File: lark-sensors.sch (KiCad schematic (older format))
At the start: 17 parts, among them IC1 MS5611-01BA03, IC2 MS5611-01BA03, U5 PCA9544AD, U9 MS5525DSO

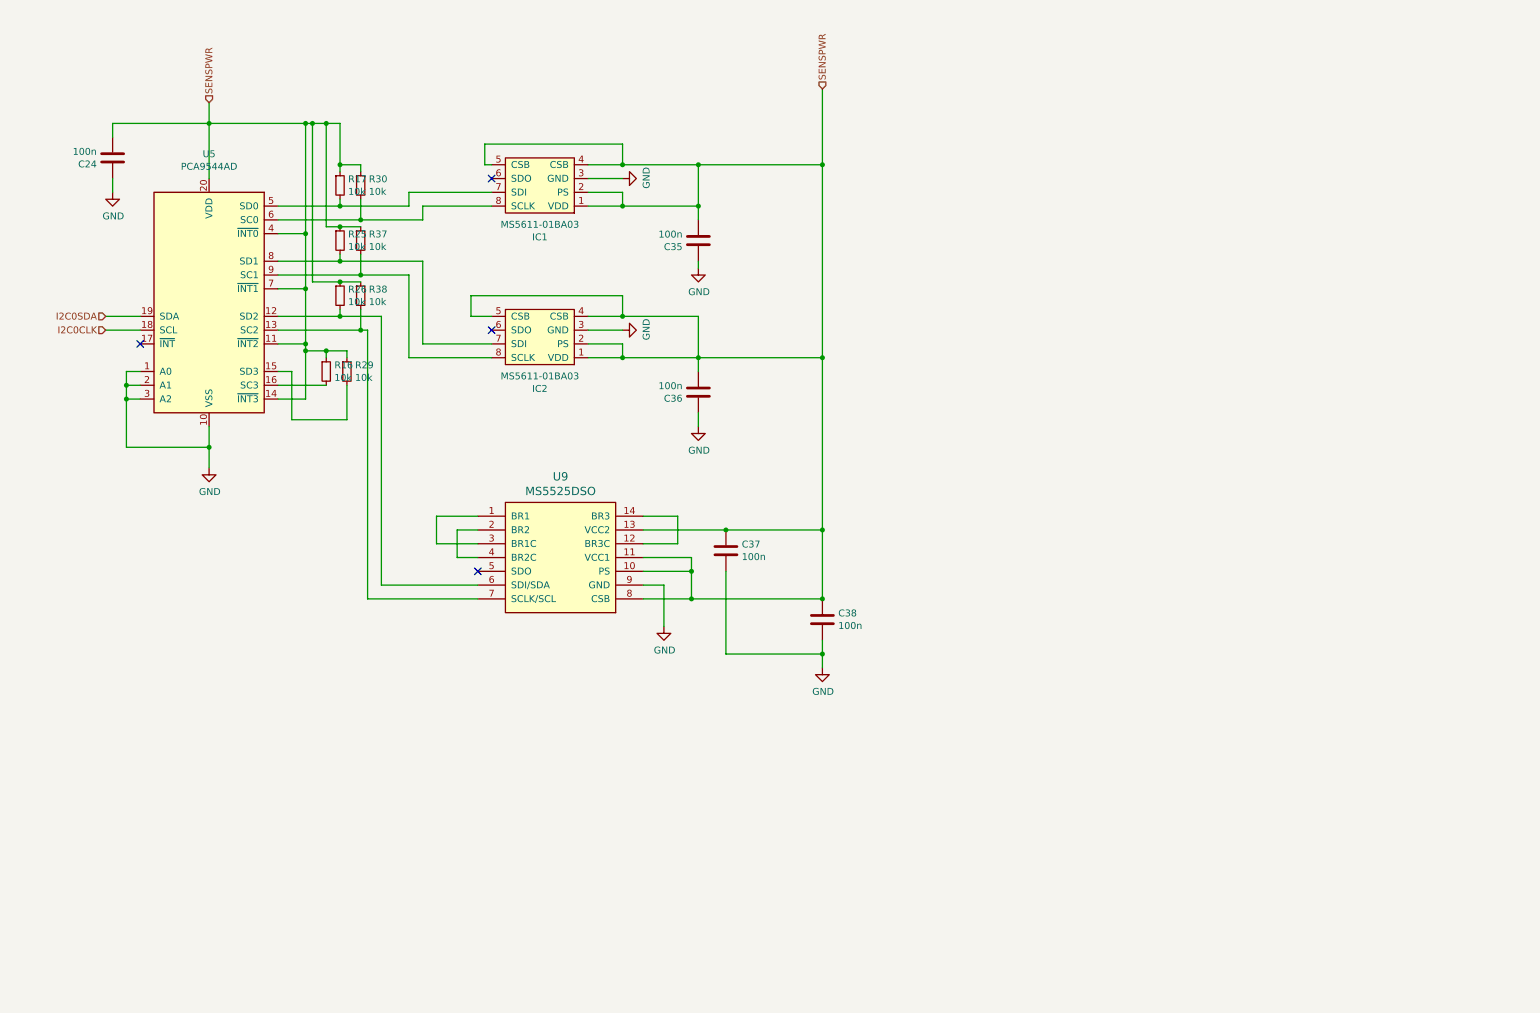
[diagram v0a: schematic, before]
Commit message: Fitting layout into 57 mm instrument.
* board width is 51 mm at the moment
* split into two boards (sensor and main) which can be stacked with
  2.54 mm pinheaders.
* ESP32 was put to bottom with optional pcb antenna facing to front.
* added footprint for optional HCLAxxE on sensorboard
* added footprint for BMI088

* Is multiple GND pins for sensor board really a good idea (ground loops)?
* Does the +12V topology make sense (especially regarding the external
  IGC ports)?
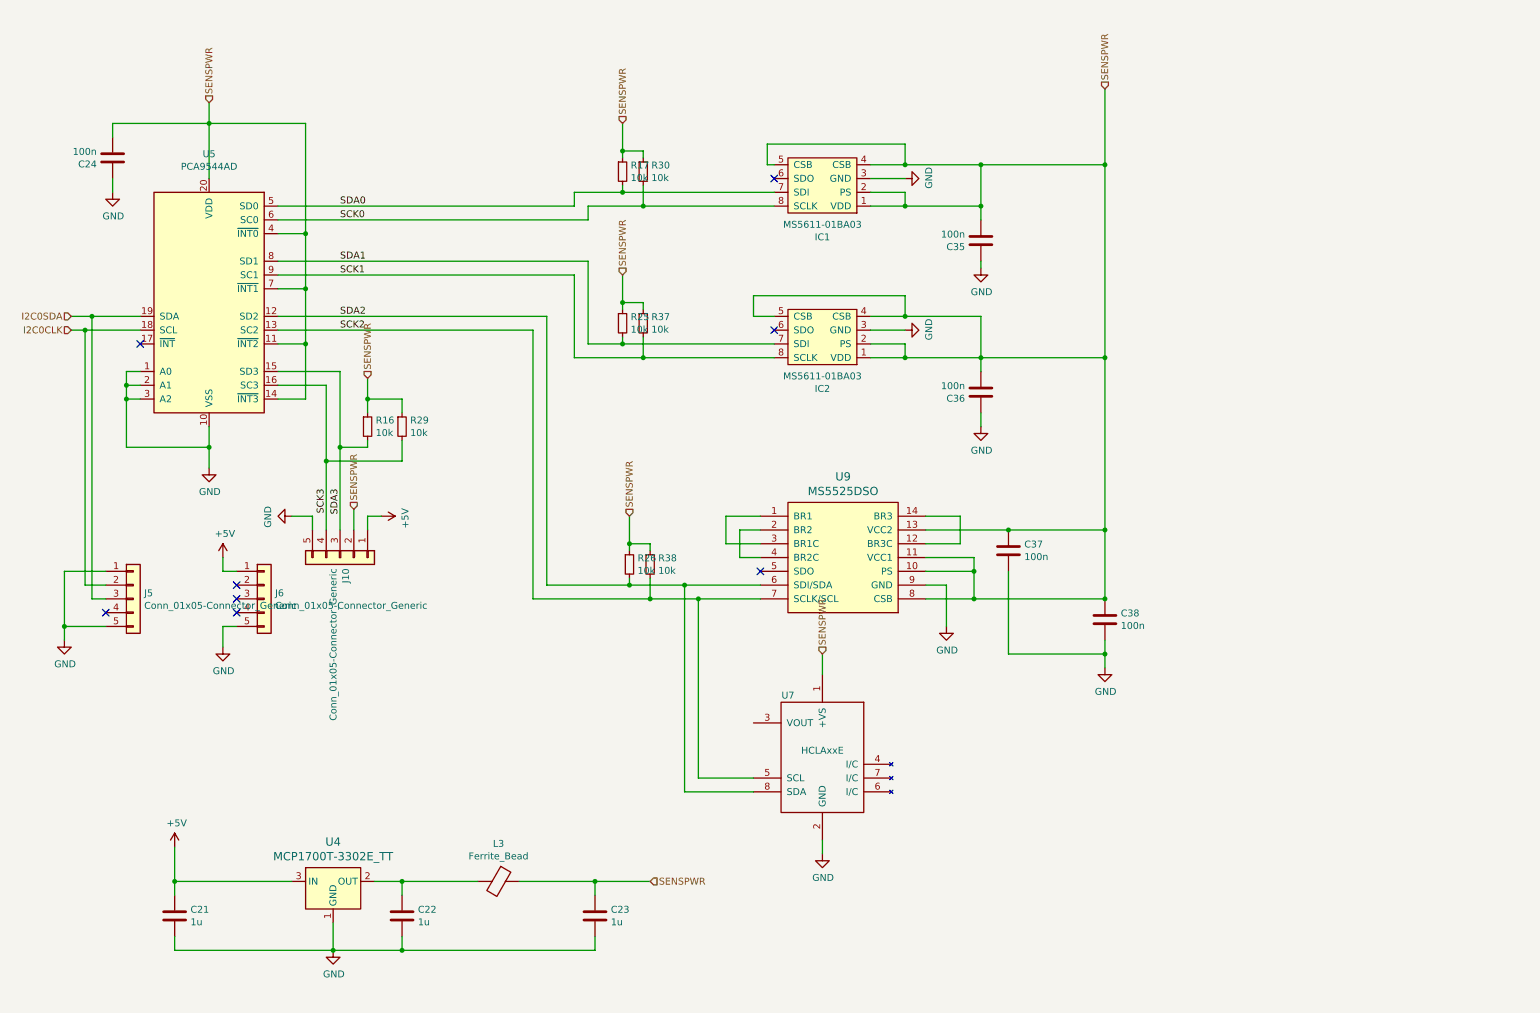
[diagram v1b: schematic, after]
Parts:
- added C21, C22, C23: 1u, Capacitor_SMD:C_0805_2012Metric_Pad1.15x1.40mm_HandSolder, symbol lark-rescue:C-Device
- added J10, J5, J6: Conn_01x05-Connector_Generic, Connector_PinHeader_2.54mm:PinHeader_1x05_P2.54mm_Vertical, symbol lark-rescue:Conn_01x05-Connector_Generic
- added L3: Ferrite_Bead, Inductor_SMD:L_0805_2012Metric_Pad1.15x1.40mm_HandSolder, symbol lark-rescue:Ferrite_Bead-Device
- added U4: MCP1700T-3302E_TT, Package_TO_SOT_SMD:SOT-23, symbol lark-rescue:MCP1700T-3302E_TT-dk_PMIC-Voltage-Regulators-Linear
- added U7: HCLAxxE, libs:HCLAxxE, symbol sensors:HCLAxxE
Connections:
- net GND: now also C21.2, C22.2, C23.2, J10.5 (Pin_5), J5.1 (Pin_1), J5.5 (Pin_5), J6.5 (Pin_5), U4.1 (GND), U7.2 (GND)
- net I2C0CLK: now also J5.2 (Pin_2)
- net I2C0SDA: now also J5.3 (Pin_3)
- net SENSPWR: now also C23.1, J10.2 (Pin_2), L3.1, U7.1 (+VS)
- net SDA2: now reaches R26.2, U5.12 (SD2), U9.6 (SDI/SDA)
- net SDA2: now also U7.8 (SDA)
- net SCK2: now reaches R38.2, U5.13 (SC2), U9.7 (SCLK/SCL)
- net SCK2: now also U7.5 (SCL)
- net SDA0: now reaches IC1.7 (SDI), R17.2, U5.5 (SD0)
- net SCK0: now reaches IC1.8 (SCLK), R30.2, U5.6 (SC0)
- net SDA1: now reaches IC2.7 (SDI), R25.2, U5.8 (SD1)
- net SCK1: now reaches IC2.8 (SCLK), R37.2, U5.9 (SC1)
- net SCK3: now reaches R29.2
- net SCK3: now also U5.16 (SC3), J10.4 (Pin_4); no longer U5.15 (SD3)
- net SDA3: now reaches R16.2
- net SDA3: now also U5.15 (SD3), J10.3 (Pin_3); no longer U5.16 (SC3)
- new net: C22.1, L3.2, U4.2 (OUT)
- new net +5V: C21.1, J10.1 (Pin_1), J6.1 (Pin_1), U4.3 (IN)
- no-connect marks 4 -> 8
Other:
- moved on the sheet: C35, C36, C37, C38, IC1, IC2, R16, R17, R25, R26, R29, R30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

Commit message: Layout almost complete.
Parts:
- removed J6: Conn_01x05-Connector_Generic, Connector_PinHeader_2.54mm:PinHeader_1x05_P2.54mm_Vertical, symbol lark-rescue:Conn_01x05-Connector_Generic
- added C3, C4: 100n, Capacitor_SMD:C_0603_1608Metric, symbol lark-rescue:C-Device
- added IC3, IC4: BMP388, libs:LGA-10_2.0x2.0x0.75_handsolder, symbol sensors:BMP388
- added J2: Conn_01x05-Connector_Generic, Connector_PinHeader_2.54mm:PinHeader_1x05_P2.54mm_Vertical, symbol lark-rescue:Conn_01x05-Connector_Generic
- added TP1: dummy-mounting-footprint, libs:lark_sensor_mount, symbol Connector:TestPoint
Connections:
- net +5V: now also J5.1 (Pin_1), J2.1 (Pin_1)
- net GND: now also C3.1, C4.1, IC3.3 (VSS_1), IC3.5 (SDO), IC3.8 (VSS_2), IC3.9 (VSS_3), IC4.3 (VSS_1), IC4.5 (SDO), IC4.8 (VSS_2), IC4.9 (VSS_3), J2.5 (Pin_5); no longer J5.1 (Pin_1)
- net I2C0CLK: now also J5.4 (Pin_4), J2.4 (Pin_4); no longer J5.2 (Pin_2)
- net I2C0SDA: now also J2.3 (Pin_3)
- net SCK0: now also IC3.2 (SCK)
- net SCK1: now also IC4.2 (SCK)
- net SDA0: now also IC3.4 (SDI)
- net SDA1: now also IC4.4 (SDI)
- net SENSPWR: now also C3.2, C4.2, IC3.1 (VDDIO), IC3.10 (VDD), IC3.6 (CSB), IC4.1 (VDDIO), IC4.10 (VDD), IC4.6 (CSB)
- no-connect marks 8 -> 7
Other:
- note added: "I2C: 0x76"
- note added: "I2C: 0x77"
- moved on the sheet: C21, C22, C23, C36, C37, C38, IC2, J5, L3, R25, R26, R37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

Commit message: sensors.sch: connect INT pins of BMP388 to I2C mux.
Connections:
- net SENSPWR: no longer U5.4 (~INT0), U5.7 (~INT1)
- net at J5.2 (Pin_2): now also J2.2 (Pin_2), U5.17 (~INT)
- net at IC3.7 (INT): now also U5.4 (~INT0)
- net at IC4.7 (INT): now also U5.7 (~INT1)
- no-connect marks 7 -> 4
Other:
- moved on the sheet: C36, C4, IC2, IC4, R25, R37

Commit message: update layout
IRQs connected
somehow handsoldering friendly BS5611

DRC is OK.
Unconnected: 5 nets (will later connect the sensor board)
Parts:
- IC1, IC2: footprint Package_LGA:LGA-8_3x5mm_P1.25mm -> libs:LGA-8_3x5mm_P1.25mm_handsolder
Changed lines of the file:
@@
 F 0 "IC1" H 6350 2075 50  0000 C CNN
 F 1 "MS5611-01BA03" H 6350 1984 50  0000 C CNN
-F 2 "Package_LGA:LGA-8_3x5mm_P1.25mm" H 6100 1350 50  0001 L CNN
+F 2 "libs:LGA-8_3x5mm_P1.25mm_handsolder" H 6100 1350 50  0001 L CNN
 F 3 "" H 6350 1750 50  0001 C CNN
 F 4 "2362662" H 6100 1250 50  0001 L CNN "Farnell"
@@
 F 0 "IC2" H 6350 4375 50  0000 C CNN
 F 1 "MS5611-01BA03" H 6350 4284 50  0000 C CNN
-F 2 "Package_LGA:LGA-8_3x5mm_P1.25mm" H 6100 3650 50  0001 L CNN
+F 2 "libs:LGA-8_3x5mm_P1.25mm_handsolder" H 6100 3650 50  0001 L CNN
 F 3 "" H 6350 4050 50  0001 C CNN
 F 4 "2362662" H 6100 3550 50  0001 L CNN "Farnell"
